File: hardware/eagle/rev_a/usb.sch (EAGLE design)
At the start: 0 parts

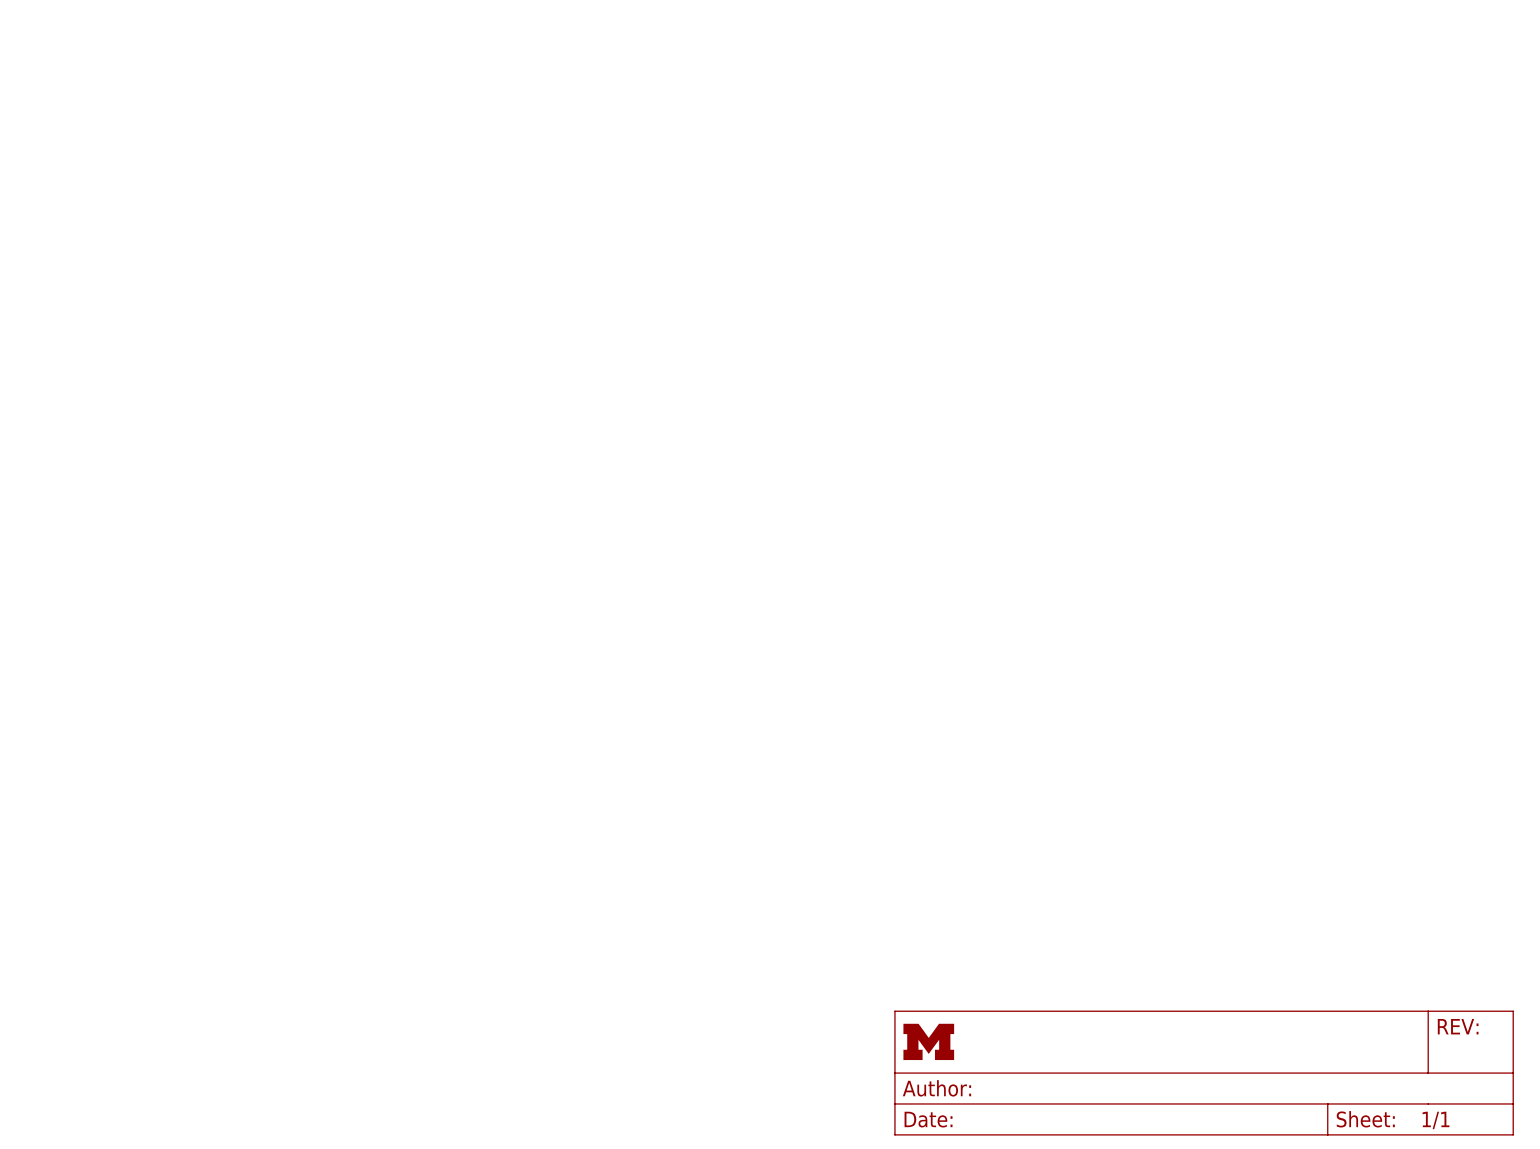
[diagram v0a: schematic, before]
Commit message: finished usb schematic
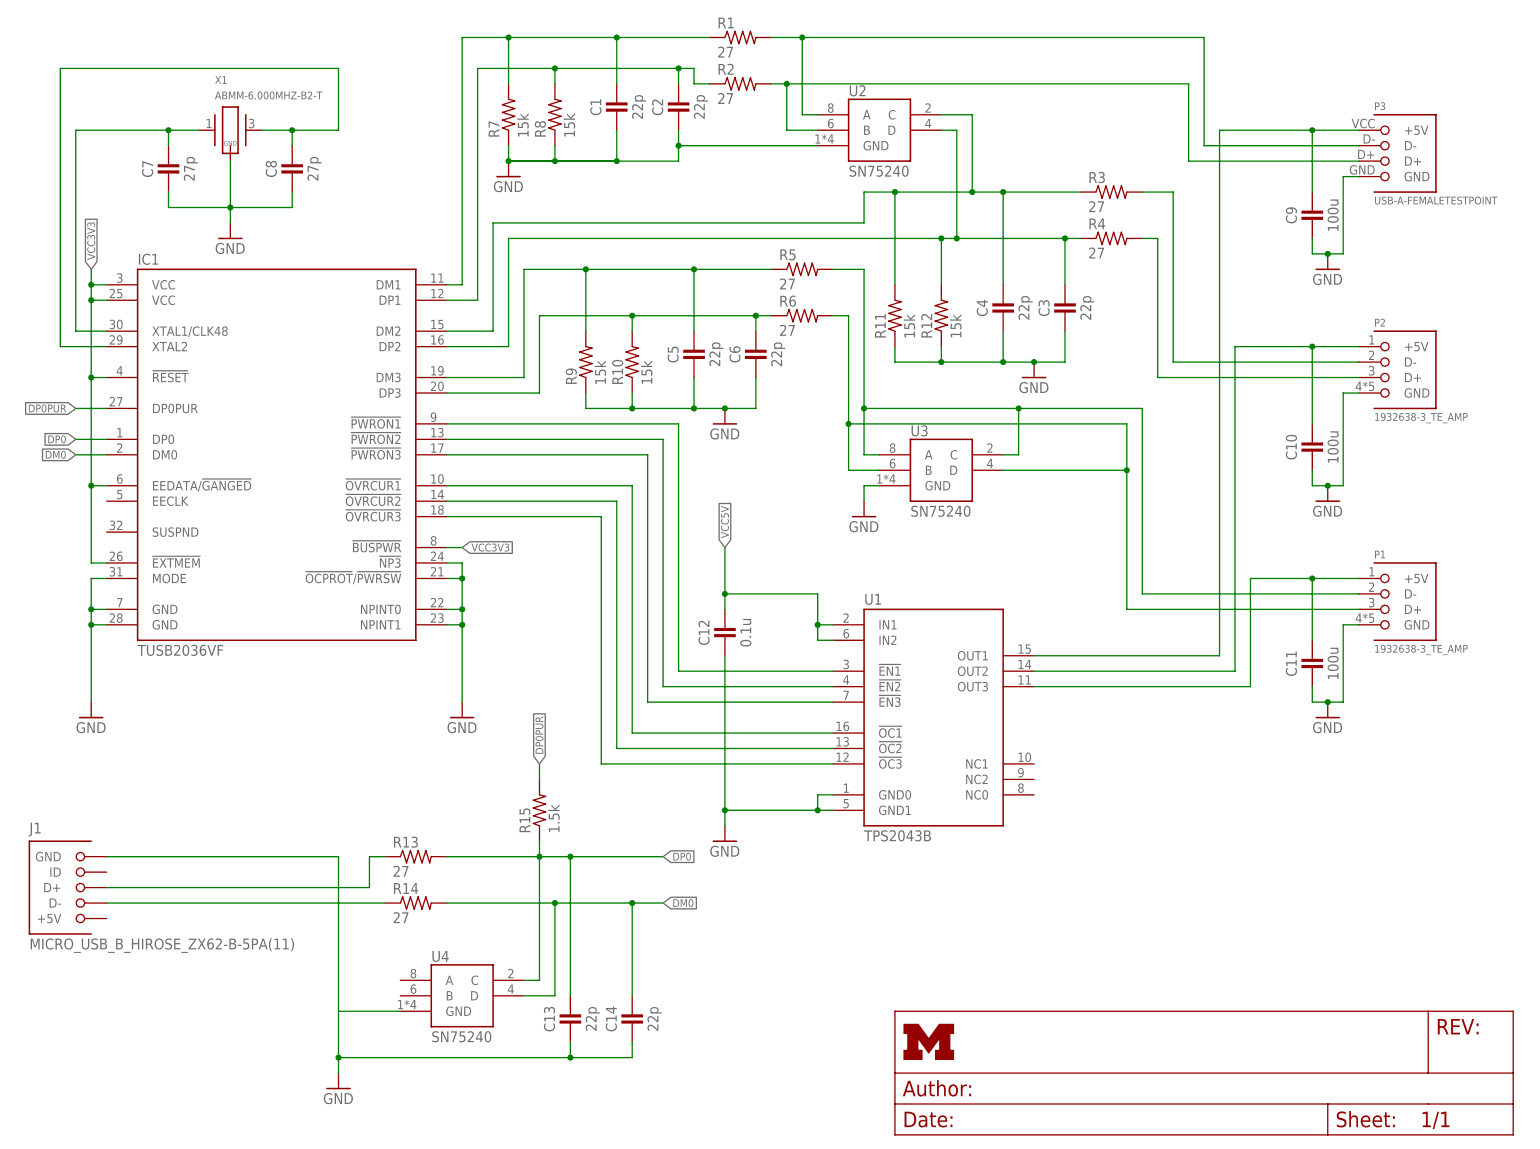
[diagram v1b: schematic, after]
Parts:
- added C1, C13, C14, C2, C3, C4, C5, C6: 22p, passives:CAPACITOR
- added C10, C11, C9: 100u, passives:CAPACITOR
- added C12: 0.1u, passives:CAPACITOR
- added C7, C8: 27p, passives:CAPACITOR
- added IC1: TUSB2036VF, BMO:TUSB2036VF
- added J1: MICRO_USB_B_HIROSE_ZX62-B-5PA(11), connector:MICRO_USB_B_HIROSE_ZX62-B-5PA(11)
- added P1, P2: 1932638-3_TE_AMP, BMO:1932638-3_TE_AMP
- added P3: USB-A-FEMALETESTPOINT, BMO:USB-A-FEMALETESTPOINT
- added R1, R13, R14, R2, R3, R4, R5, R6: 27, passives:RESISTOR0402_RES
- added R10, R11, R12, R7, R8, R9: 15k, passives:RESISTOR0402_RES
- added R15: 1.5k, passives:RESISTOR0402_RES
- added U1: TPS2043B, BMO:TPS2043B
- added U2, U3, U4: SN75240, BMO:SN75240
- added X1: ABMM-6.000MHZ-B2-T, BMO:ABMM-6.000MHZ-B2-T
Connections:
- new net DM0: C14.1, IC1.DM0, R14.2, U4.D
- new net DP0: C13.1, IC1.DP0, R13.2, R15.1, U4.C
- new net DP0PUR: IC1.DP0PUR, R15.2
- new net GND: C1.2, C10.2, C11.2, C12.2, C13.2, C14.2, C2.2, C3.2, C4.2, C5.2, C6.2, C7.2, C8.2, C9.2, IC1.!NP3, IC1.!OCPROT!/!PWRSW!, IC1.GND@1, IC1.GND@2, IC1.MODE, IC1.NPINT0, IC1.NPINT1, J1.GND, P1.GND, P2.GND, P3.GND, R10.1, R11.1, R12.1, R7.1, R8.1, R9.1, U1.GND0, U1.GND1, U2.GND, U3.GND, U4.GND, X1.GND
- new net N$1: C7.1, IC1.XTAL1/CLK48, X1.1
- new net N$10: P2.D-, R3.2
- new net N$11: P3.D+, R2.2, U2.B
- new net N$12: P3.D-, R1.2, U2.A
- new net N$13: IC1.!PWRON1, U1.!EN1
- new net N$14: IC1.!PWRON2, U1.!EN2
- new net N$15: IC1.!PWRON3, U1.!EN3
- new net N$16: C1.1, IC1.DM1, R1.1, R7.2
- new net N$17: IC1.!OVRCUR1, U1.!OC1
- new net N$18: C2.1, IC1.DP1, R2.1, R8.2
- new net N$19: IC1.!OVRCUR2, U1.!OC2
- new net N$2: C8.1, IC1.XTAL2, X1.2
- new net N$20: C5.1, IC1.DM3, R5.1, R9.2
- new net N$21: IC1.!OVRCUR3, U1.!OC3
- new net N$22: C6.1, IC1.DP3, R10.2, R6.1
- new net N$24: C4.1, IC1.DM2, R11.2, R3.1, U2.C
- new net N$25: C3.1, IC1.DP2, R12.2, R4.1, U2.D
- new net N$26: J1.D-, R14.1
- new net N$27: J1.D+, R13.1
- new net N$3: C11.1, P1.+5V, U1.OUT3
- new net N$4: C10.1, P2.+5V, U1.OUT2
- new net N$5: C9.1, P3.+5V, U1.OUT1
- new net N$7: P1.D-, R5.2, U3.A, U3.C
- new net N$8: P1.D+, R6.2, U3.B, U3.D
- new net N$9: P2.D+, R4.2
- new net VCC3V3: IC1.!BUSPWR, IC1.!EXTMEM, IC1.!RESET, IC1.EEDATA/!GANGED, IC1.VCC@1, IC1.VCC@2
- new net VCC5V: C12.1, U1.IN1, U1.IN2

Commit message: tweaking size, added power header
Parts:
- added C15: 0.1u, passives:CAPACITOR
- added JP1: (no value), SparkFun-Connectors:M03PTH
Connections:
- net GND: now also C15.2, JP1.1
- net VCC3V3: now also C15.1, JP1.3
- net VCC5V: now also JP1.2
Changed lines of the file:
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@@
 <layer number="144" name="Drill_legend" color="7" fill="1" visible="no" active="yes"/>
 <layer number="151" name="HeatSink" color="7" fill="1" visible="no" active="yes"/>
+<layer number="199" name="Contour" color="7" fill="1" visible="yes" active="yes"/>
 <layer number="200" name="200bmp" color="1" fill="10" visible="yes" active="yes"/>
 <layer number="201" name="201bmp" color="1" fill="10" visible="yes" active="yes"/>
@@
 <schematic xreflabel="%F%N/%S.%C%R" xrefpart="/%S.%C%R">
 <attributes>
+<attribute name="AUTHOR" value="Neal Jackson"/>
+<attribute name="REV" value="A"/>
+<attribute name="TITLE" value="BMO USB"/>
 </attributes>
 <variantdefs>
@@
 <part name="U4" library="BMO" deviceset="SN75240" device=""/>
 <part name="R15" library="passives" deviceset="RESISTOR" device="0402_RES" value="1.5k"/>
+<part name="JP1" library="SparkFun-Connectors" deviceset="M03" device="PTH"/>
+<part name="C15" library="passives" deviceset="CAPACITOR" device="" value="0.1u"/>
 </parts>
 <sheets>
@@
 <instance part="U4" gate="G$1" x="71.12" y="17.78"/>
 <instance part="R15" gate="G$1" x="88.9" y="53.34" rot="R90"/>
+<instance part="JP1" gate="G$1" x="190.5" y="43.18"/>
+<instance part="C15" gate="G$1" x="7.62" y="96.52"/>
 </instances>
 <busses>
@@
 <wire x1="15.24" y1="91.44" x2="15.24" y2="86.36" width="0.1524" layer="91"/>
 <junction x="15.24" y="86.36"/>
+<pinref part="C15" gate="G$1" pin="2"/>
+<wire x1="7.62" y1="91.44" x2="7.62" y2="83.82" width="0.1524" layer="91"/>
+<wire x1="7.62" y1="83.82" x2="15.24" y2="83.82" width="0.1524" layer="91"/>
 </segment>
 <segment>
@@
 <wire x1="66.04" y1="20.32" x2="55.88" y2="20.32" width="0.1524" layer="91"/>
 </segment>
+<segment>
+<pinref part="JP1" gate="G$1" pin="1"/>
+<wire x1="198.12" y1="40.64" x2="200.66" y2="40.64" width="0.1524" layer="91"/>
+<label x="200.66" y="40.64" size="1.27" layer="95" xref="yes"/>
+</segment>
 </net>
 <net name="N$7" class="0">
@@
 <junction x="134.62" y="83.82"/>
 </segment>
+<segment>
+<pinref part="JP1" gate="G$1" pin="2"/>
+<wire x1="198.12" y1="43.18" x2="200.66" y2="43.18" width="0.1524" layer="91"/>
+<label x="200.66" y="43.18" size="1.27" layer="95" xref="yes"/>
+</segment>
 </net>
 <net name="VCC3V3" class="0">
@@
 <wire x1="17.78" y1="106.68" x2="15.24" y2="106.68" width="0.1524" layer="91"/>
 <junction x="15.24" y="106.68"/>
+<wire x1="15.24" y1="106.68" x2="7.62" y2="106.68" width="0.1524" layer="91"/>
+<wire x1="7.62" y1="106.68" x2="7.62" y2="99.06" width="0.1524" layer="91"/>
+<pinref part="C15" gate="G$1" pin="1"/>
 </segment>
 <segment>
@@
 <label x="76.2" y="96.52" size="1.27" layer="95" xref="yes"/>
 </segment>
-</net>
+<segment>
+<pinref part="JP1" gate="G$1" pin="3"/>
+<wire x1="198.12" y1="45.72" x2="200.66" y2="45.72" width="0.1524" layer="91"/>
+<label x="200.66" y="45.72" size="1.27" layer="95" xref="yes"/>
+</segment>
+</net>

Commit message: Fitted board to case, added silkscreen
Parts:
- renumbered IC1 to U5
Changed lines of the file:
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@@
 <parts>
 <part name="FRAME1" library="frames" deviceset="LETTER_L" device=""/>
-<part name="IC1" library="BMO" deviceset="TUSB2036VF" device=""/>
+<part name="U5" library="BMO" deviceset="TUSB2036VF" device=""/>
 <part name="U1" library="BMO" deviceset="TPS2043B" device=""/>
 <part name="P1" library="BMO" deviceset="1932638-3_TE_AMP" device=""/>
@@
 <instance part="FRAME1" gate="G$1" x="0" y="0"/>
 <instance part="FRAME1" gate="G$2" x="147.32" y="0"/>
-<instance part="IC1" gate="A" x="45.72" y="111.76"/>
+<instance part="U5" gate="A" x="45.72" y="111.76"/>
 <instance part="U1" gate="G$1" x="142.24" y="50.8"/>
 <instance part="P1" gate="G$1" x="228.6" y="86.36"/>
@@
 <net name="GND" class="0">
 <segment>
-<pinref part="IC1" gate="A" pin="GND@2"/>
+<pinref part="U5" gate="A" pin="GND@2"/>
 <wire x1="15.24" y1="83.82" x2="17.78" y2="83.82" width="0.1524" layer="91"/>
-<pinref part="IC1" gate="A" pin="GND@1"/>
+<pinref part="U5" gate="A" pin="GND@1"/>
 <wire x1="17.78" y1="86.36" x2="15.24" y2="86.36" width="0.1524" layer="91"/>
 <wire x1="15.24" y1="86.36" x2="15.24" y2="83.82" width="0.1524" layer="91"/>
@@
 <wire x1="15.24" y1="71.12" x2="15.24" y2="83.82" width="0.1524" layer="91"/>
 <pinref part="GND1" gate="1" pin="GND"/>
-<pinref part="IC1" gate="A" pin="MODE"/>
+<pinref part="U5" gate="A" pin="MODE"/>
 <wire x1="17.78" y1="91.44" x2="15.24" y2="91.44" width="0.1524" layer="91"/>
 <wire x1="15.24" y1="91.44" x2="15.24" y2="86.36" width="0.1524" layer="91"/>
@@
 </segment>
 <segment>
-<pinref part="IC1" gate="A" pin="NPINT1"/>
+<pinref part="U5" gate="A" pin="NPINT1"/>
 <wire x1="73.66" y1="83.82" x2="76.2" y2="83.82" width="0.1524" layer="91"/>
-<pinref part="IC1" gate="A" pin="NPINT0"/>
+<pinref part="U5" gate="A" pin="NPINT0"/>
 <wire x1="73.66" y1="86.36" x2="76.2" y2="86.36" width="0.1524" layer="91"/>
-<pinref part="IC1" gate="A" pin="!OCPROT!/!PWRSW!"/>
+<pinref part="U5" gate="A" pin="!OCPROT!/!PWRSW!"/>
 <wire x1="73.66" y1="91.44" x2="76.2" y2="91.44" width="0.1524" layer="91"/>
-<pinref part="IC1" gate="A" pin="!NP3"/>
+<pinref part="U5" gate="A" pin="!NP3"/>
 <wire x1="73.66" y1="93.98" x2="76.2" y2="93.98" width="0.1524" layer="91"/>
 <wire x1="76.2" y1="93.98" x2="76.2" y2="91.44" width="0.1524" layer="91"/>
@@
 <net name="N$16" class="0">
 <segment>
-<pinref part="IC1" gate="A" pin="DM1"/>
+<pinref part="U5" gate="A" pin="DM1"/>
 <wire x1="73.66" y1="139.7" x2="76.2" y2="139.7" width="0.1524" layer="91"/>
 <pinref part="R1" gate="G$1" pin="1"/>
@@
 <net name="N$18" class="0">
 <segment>
-<pinref part="IC1" gate="A" pin="DP1"/>
+<pinref part="U5" gate="A" pin="DP1"/>
 <wire x1="73.66" y1="137.16" x2="78.74" y2="137.16" width="0.1524" layer="91"/>
 <pinref part="R2" gate="G$1" pin="1"/>
@@
 <segment>
 <wire x1="86.36" y1="124.46" x2="86.36" y2="142.24" width="0.1524" layer="91"/>
-<pinref part="IC1" gate="A" pin="DM3"/>
+<pinref part="U5" gate="A" pin="DM3"/>
 <wire x1="73.66" y1="124.46" x2="86.36" y2="124.46" width="0.1524" layer="91"/>
 <wire x1="86.36" y1="142.24" x2="96.52" y2="142.24" width="0.1524" layer="91"/>
@@
 <net name="N$22" class="0">
 <segment>
-<pinref part="IC1" gate="A" pin="DP3"/>
+<pinref part="U5" gate="A" pin="DP3"/>
 <wire x1="88.9" y1="134.62" x2="88.9" y2="121.92" width="0.1524" layer="91"/>
 <wire x1="88.9" y1="121.92" x2="73.66" y2="121.92" width="0.1524" layer="91"/>
@@
 <pinref part="C4" gate="G$1" pin="1"/>
 <wire x1="165.1" y1="139.7" x2="165.1" y2="154.94" width="0.1524" layer="91"/>
-<pinref part="IC1" gate="A" pin="DM2"/>
+<pinref part="U5" gate="A" pin="DM2"/>
 <wire x1="81.28" y1="132.08" x2="73.66" y2="132.08" width="0.1524" layer="91"/>
 <pinref part="R3" gate="G$1" pin="1"/>
@@
 <pinref part="C3" gate="G$1" pin="1"/>
 <wire x1="175.26" y1="139.7" x2="175.26" y2="147.32" width="0.1524" layer="91"/>
-<pinref part="IC1" gate="A" pin="DP2"/>
+<pinref part="U5" gate="A" pin="DP2"/>
 <wire x1="73.66" y1="129.54" x2="83.82" y2="129.54" width="0.1524" layer="91"/>
 <wire x1="83.82" y1="129.54" x2="83.82" y2="147.32" width="0.1524" layer="91"/>
@@
 <net name="N$13" class="0">
 <segment>
-<pinref part="IC1" gate="A" pin="!PWRON1"/>
+<pinref part="U5" gate="A" pin="!PWRON1"/>
 <wire x1="73.66" y1="116.84" x2="111.76" y2="116.84" width="0.1524" layer="91"/>
 <wire x1="111.76" y1="116.84" x2="111.76" y2="76.2" width="0.1524" layer="91"/>
@@
 <wire x1="137.16" y1="73.66" x2="109.22" y2="73.66" width="0.1524" layer="91"/>
 <wire x1="109.22" y1="73.66" x2="109.22" y2="114.3" width="0.1524" layer="91"/>
-<pinref part="IC1" gate="A" pin="!PWRON2"/>
+<pinref part="U5" gate="A" pin="!PWRON2"/>
 <wire x1="109.22" y1="114.3" x2="73.66" y2="114.3" width="0.1524" layer="91"/>
 </segment>
@@
 <net name="N$15" class="0">
 <segment>
-<pinref part="IC1" gate="A" pin="!PWRON3"/>
+<pinref part="U5" gate="A" pin="!PWRON3"/>
 <wire x1="73.66" y1="111.76" x2="106.68" y2="111.76" width="0.1524" layer="91"/>
 <wire x1="106.68" y1="111.76" x2="106.68" y2="71.12" width="0.1524" layer="91"/>
@@
 <net name="N$17" class="0">
 <segment>
-<pinref part="IC1" gate="A" pin="!OVRCUR1"/>
+<pinref part="U5" gate="A" pin="!OVRCUR1"/>
 <wire x1="73.66" y1="106.68" x2="104.14" y2="106.68" width="0.1524" layer="91"/>
 <wire x1="104.14" y1="106.68" x2="104.14" y2="66.04" width="0.1524" layer="91"/>
@@
 <net name="N$19" class="0">
 <segment>
-<pinref part="IC1" gate="A" pin="!OVRCUR2"/>
+<pinref part="U5" gate="A" pin="!OVRCUR2"/>
 <wire x1="73.66" y1="104.14" x2="101.6" y2="104.14" width="0.1524" layer="91"/>
 <wire x1="101.6" y1="104.14" x2="101.6" y2="63.5" width="0.1524" layer="91"/>
@@
 <net name="N$21" class="0">
 <segment>
-<pinref part="IC1" gate="A" pin="!OVRCUR3"/>
+<pinref part="U5" gate="A" pin="!OVRCUR3"/>
 <wire x1="73.66" y1="101.6" x2="99.06" y2="101.6" width="0.1524" layer="91"/>
 <wire x1="99.06" y1="101.6" x2="99.06" y2="60.96" width="0.1524" layer="91"/>
@@
 <net name="VCC3V3" class="0">
 <segment>
-<pinref part="IC1" gate="A" pin="VCC@1"/>
+<pinref part="U5" gate="A" pin="VCC@1"/>
 <wire x1="17.78" y1="139.7" x2="15.24" y2="139.7" width="0.1524" layer="91"/>
 <wire x1="15.24" y1="139.7" x2="15.24" y2="142.24" width="0.1524" layer="91"/>
-<pinref part="IC1" gate="A" pin="VCC@2"/>
+<pinref part="U5" gate="A" pin="VCC@2"/>
 <wire x1="17.78" y1="137.16" x2="15.24" y2="137.16" width="0.1524" layer="91"/>
 <wire x1="15.24" y1="137.16" x2="15.24" y2="139.7" width="0.1524" layer="91"/>
 <junction x="15.24" y="139.7"/>
 <label x="15.24" y="142.24" size="1.27" layer="95" rot="R90" xref="yes"/>
-<pinref part="IC1" gate="A" pin="!RESET"/>
+<pinref part="U5" gate="A" pin="!RESET"/>
 <wire x1="17.78" y1="124.46" x2="15.24" y2="124.46" width="0.1524" layer="91"/>
 <wire x1="15.24" y1="124.46" x2="15.24" y2="137.16" width="0.1524" layer="91"/>
 <junction x="15.24" y="137.16"/>
-<pinref part="IC1" gate="A" pin="!EXTMEM"/>
+<pinref part="U5" gate="A" pin="!EXTMEM"/>
 <wire x1="17.78" y1="93.98" x2="15.24" y2="93.98" width="0.1524" layer="91"/>
 <wire x1="15.24" y1="93.98" x2="15.24" y2="106.68" width="0.1524" layer="91"/>
 <junction x="15.24" y="124.46"/>
-<pinref part="IC1" gate="A" pin="EEDATA/!GANGED"/>
+<pinref part="U5" gate="A" pin="EEDATA/!GANGED"/>
 <wire x1="15.24" y1="106.68" x2="15.24" y2="124.46" width="0.1524" layer="91"/>
 <wire x1="17.78" y1="106.68" x2="15.24" y2="106.68" width="0.1524" layer="91"/>
@@
 </segment>
 <segment>
-<pinref part="IC1" gate="A" pin="!BUSPWR"/>
+<pinref part="U5" gate="A" pin="!BUSPWR"/>
 <wire x1="73.66" y1="96.52" x2="76.2" y2="96.52" width="0.1524" layer="91"/>
 <label x="76.2" y="96.52" size="1.27" layer="95" xref="yes"/>
@@
 <net name="N$1" class="0">
 <segment>
-<pinref part="IC1" gate="A" pin="XTAL1/CLK48"/>
+<pinref part="U5" gate="A" pin="XTAL1/CLK48"/>
 <wire x1="17.78" y1="132.08" x2="12.7" y2="132.08" width="0.1524" layer="91"/>
 <wire x1="12.7" y1="132.08" x2="12.7" y2="165.1" width="0.1524" layer="91"/>
@@
 <net name="N$2" class="0">
 <segment>
-<pinref part="IC1" gate="A" pin="XTAL2"/>
+<pinref part="U5" gate="A" pin="XTAL2"/>
 <wire x1="17.78" y1="129.54" x2="10.16" y2="129.54" width="0.1524" layer="91"/>
 <wire x1="10.16" y1="129.54" x2="10.16" y2="175.26" width="0.1524" layer="91"/>
@@
 <net name="DP0PUR" class="0">
 <segment>
-<pinref part="IC1" gate="A" pin="DP0PUR"/>
+<pinref part="U5" gate="A" pin="DP0PUR"/>
 <wire x1="17.78" y1="119.38" x2="12.7" y2="119.38" width="0.1524" layer="91"/>
 <label x="12.7" y="119.38" size="1.27" layer="95" rot="R180" xref="yes"/>
@@
 <net name="DP0" class="0">
 <segment>
-<pinref part="IC1" gate="A" pin="DP0"/>
+<pinref part="U5" gate="A" pin="DP0"/>
 <wire x1="17.78" y1="114.3" x2="12.7" y2="114.3" width="0.1524" layer="91"/>
 <label x="12.7" y="114.3" size="1.27" layer="95" rot="R180" xref="yes"/>
@@
 <net name="DM0" class="0">
 <segment>
-<pinref part="IC1" gate="A" pin="DM0"/>
+<pinref part="U5" gate="A" pin="DM0"/>
 <wire x1="17.78" y1="111.76" x2="12.7" y2="111.76" width="0.1524" layer="91"/>
 <label x="12.7" y="111.76" size="1.27" layer="95" rot="R180" xref="yes"/>
